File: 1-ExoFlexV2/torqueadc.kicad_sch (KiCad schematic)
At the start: 81 parts, among them J68 Jumper, J69 Jumper, J70 Jumper, J87 Jumper, J88 Jumper, J89 Jumper, U33 OP_AMP2, U34 OP_AMP2, U35 OP_AMP2, U36 OP_AMP2, U37 OP_AMP2, U38 OP_AMP2, U39 OP_AMP2, U40 OP_AMP2, U41 OP_AMP2

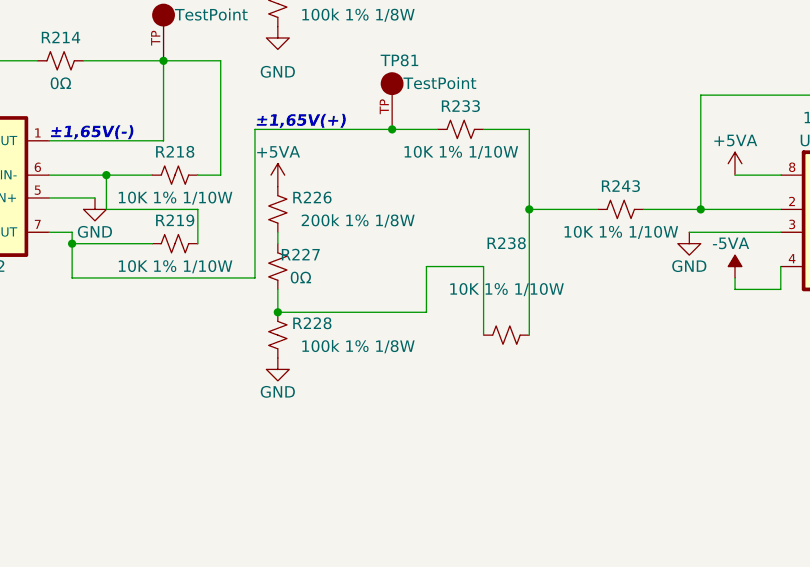
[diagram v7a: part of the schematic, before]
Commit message: Placement 1
- Placement de tous les connecteur
- Placement de tous les test point
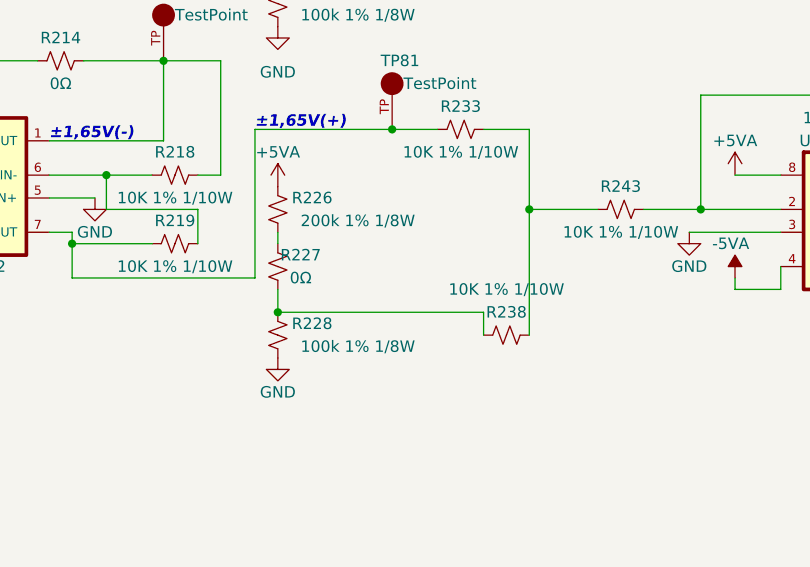
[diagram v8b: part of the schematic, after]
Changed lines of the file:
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@@
     (stroke (width 0) (type default) (color 0 0 0 0))
   )
-  (wire (pts (xy 100.33 124.46) (xy 83.82 124.46))
+  (wire (pts (xy 83.82 124.46) (xy 106.68 124.46))
     (stroke (width 0) (type default) (color 0 0 0 0))
   )
@@
     (stroke (width 0) (type default) (color 0 0 0 0))
   )
-  (wire (pts (xy 106.68 119.38) (xy 106.68 127))
+  (wire (pts (xy 106.68 124.46) (xy 106.68 127))
     (stroke (width 0) (type default) (color 0 0 0 0))
   )
@@
     (stroke (width 0) (type default) (color 0 0 0 0))
   )
-  (wire (pts (xy 100.33 119.38) (xy 106.68 119.38))
-    (stroke (width 0) (type default) (color 0 0 0 0))
-  )
   (wire (pts (xy 229.87 100.33) (xy 229.87 104.14))
     (stroke (width 0) (type default) (color 0 0 0 0))
@@
     (stroke (width 0) (type default) (color 0 0 0 0))
   )
-  (wire (pts (xy 100.33 119.38) (xy 100.33 124.46))
-    (stroke (width 0) (type default) (color 0 0 0 0))
-  )
   (wire (pts (xy 146.05 100.33) (xy 130.81 100.33))
     (stroke (width 0) (type default) (color 0 0 0 0))
@@
   (symbol (lib_id "Device:R_Small_US") (at 109.22 127 90) (unit 1)
     (in_bom yes) (on_board yes)
-    (property "Reference" "R238" (id 0) (at 109.22 116.84 90))
+    (property "Reference" "R238" (id 0) (at 109.22 124.46 90))
     (property "Value" "10K 1% 1/10W" (id 1) (at 109.22 121.92 90))
     (property "Footprint" "Resistor_SMD:R_0603_1608Metric" (id 2) (at 109.22 127 0)
